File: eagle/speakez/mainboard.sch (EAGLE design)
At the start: 15 parts

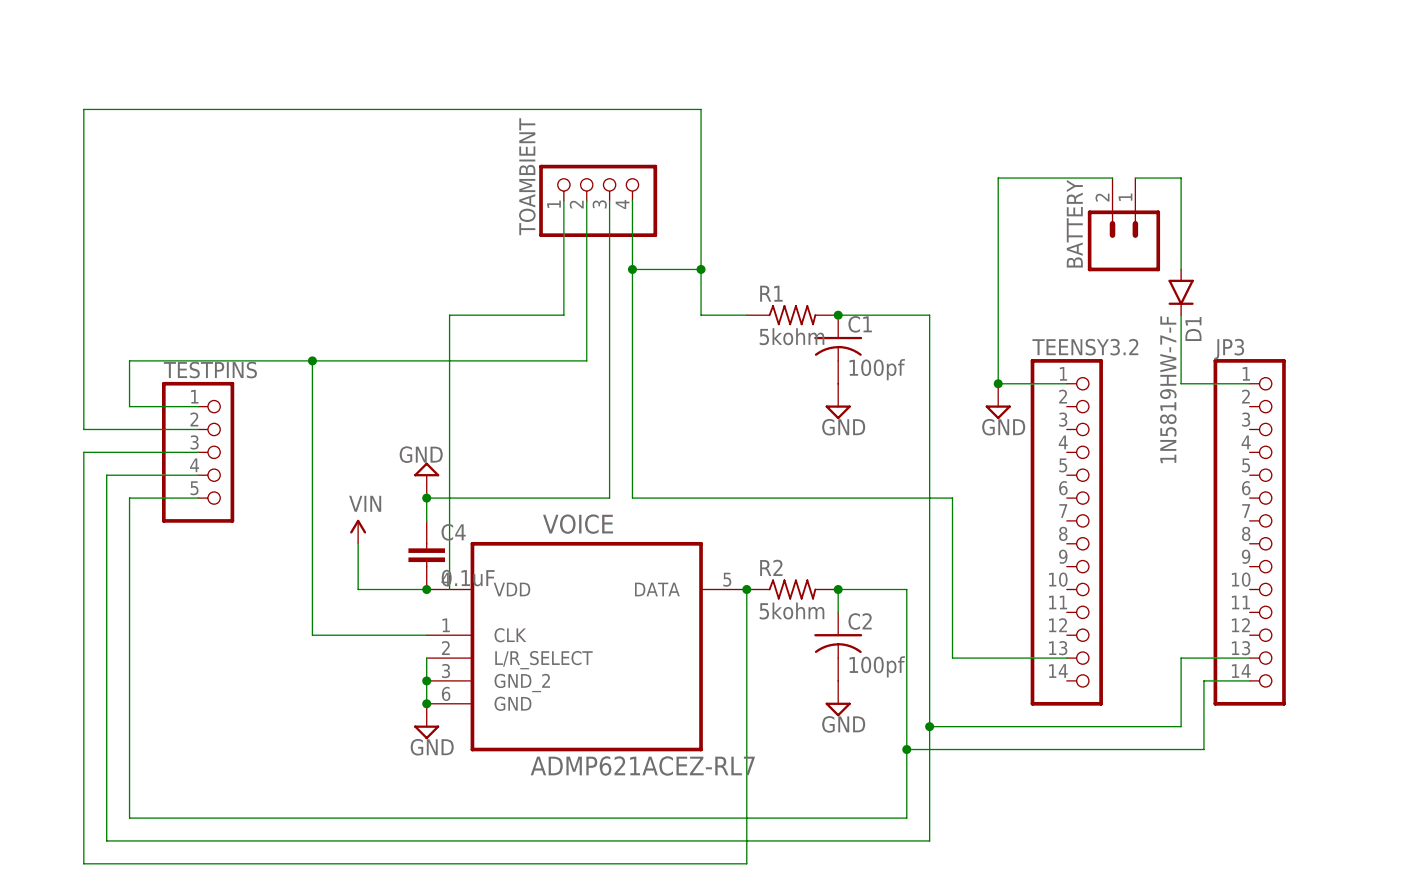
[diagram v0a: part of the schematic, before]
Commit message: remap teensy pins
move analog inputs to adc pins, switch 3.3v source, gnd source. add clk
signal to digital output pin
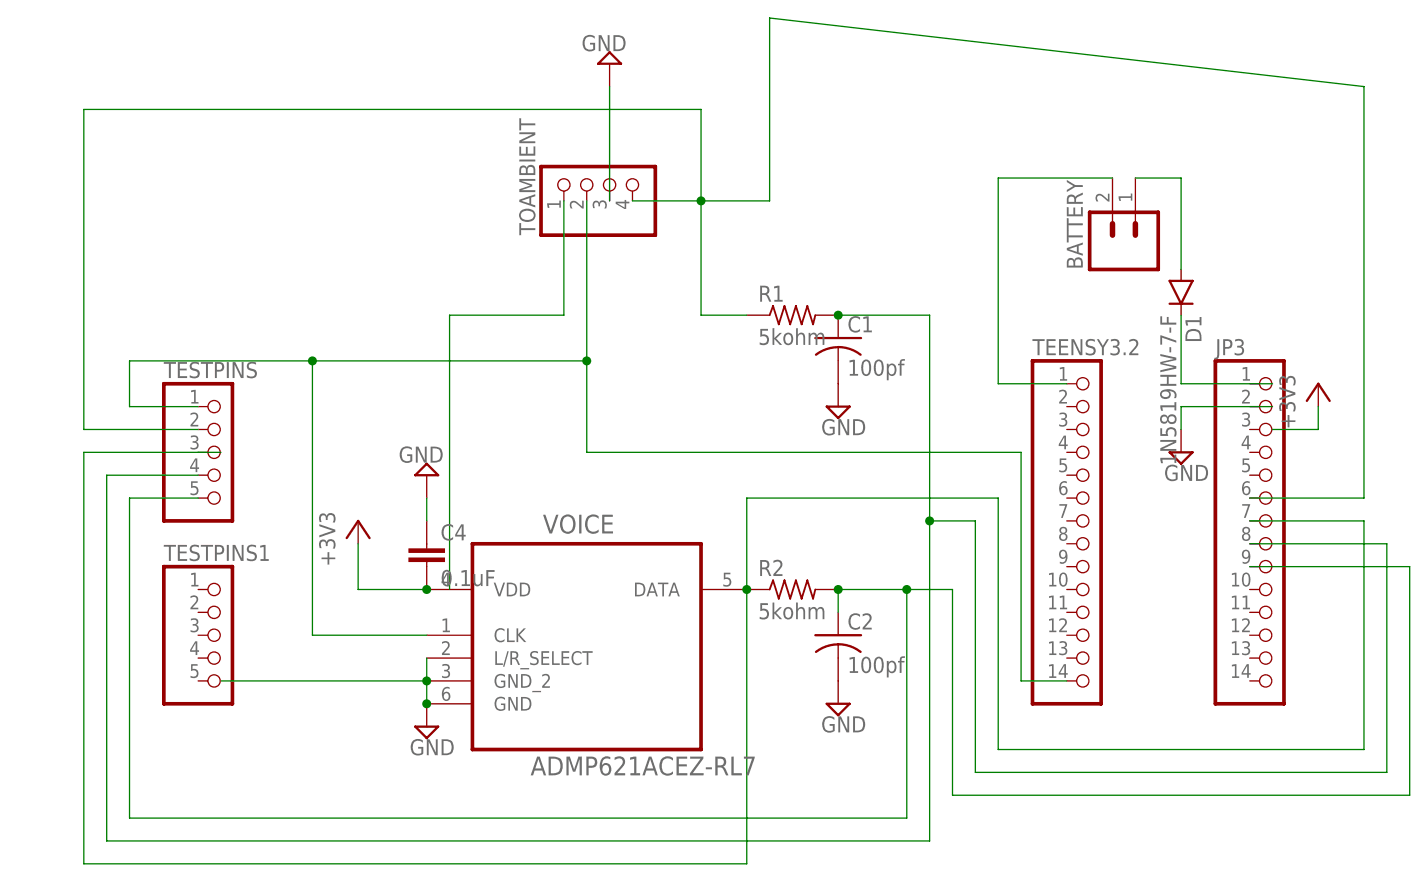
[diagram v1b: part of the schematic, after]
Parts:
- added TESTPINS1: (no value), pinhead:PINHD-1X5M
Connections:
- net VIN renamed +3V3
- new net N$13: BATTERY.2, TEENSY3.2.1
- net GND: no longer BATTERY.2, TEENSY3.2.1
- net N$1: now also JP3.8; no longer JP3.13
- net N$10: now also JP3.6; no longer TEENSY3.2.13
- net N$2: now also JP3.9; no longer JP3.14
- net N$3: no longer JP3.1
- net N$4: now also JP3.7
- net TEST-PINS: now also TEENSY3.2.14

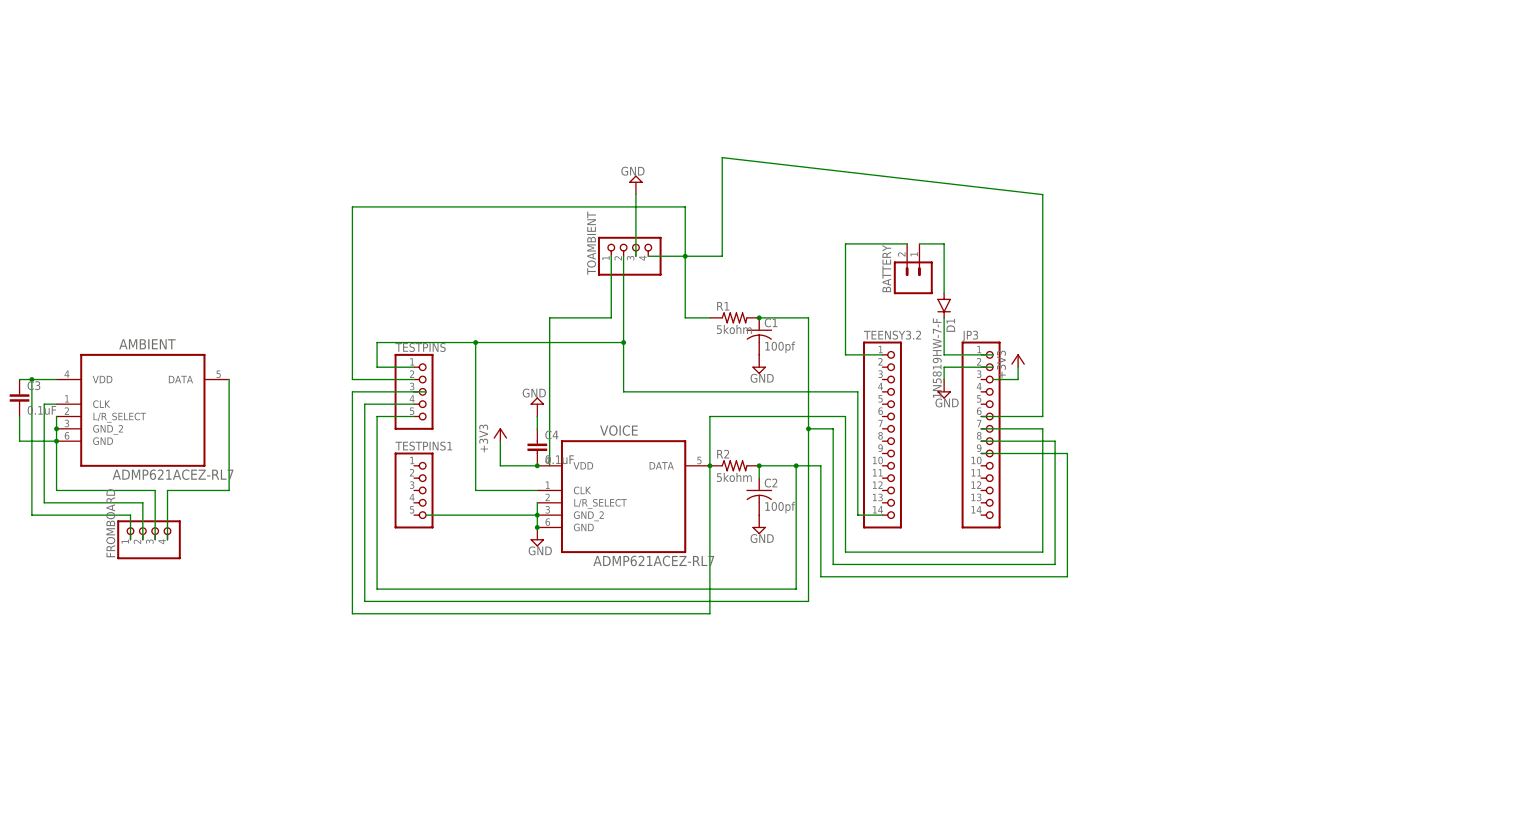
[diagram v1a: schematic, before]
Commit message: Added microcontroller
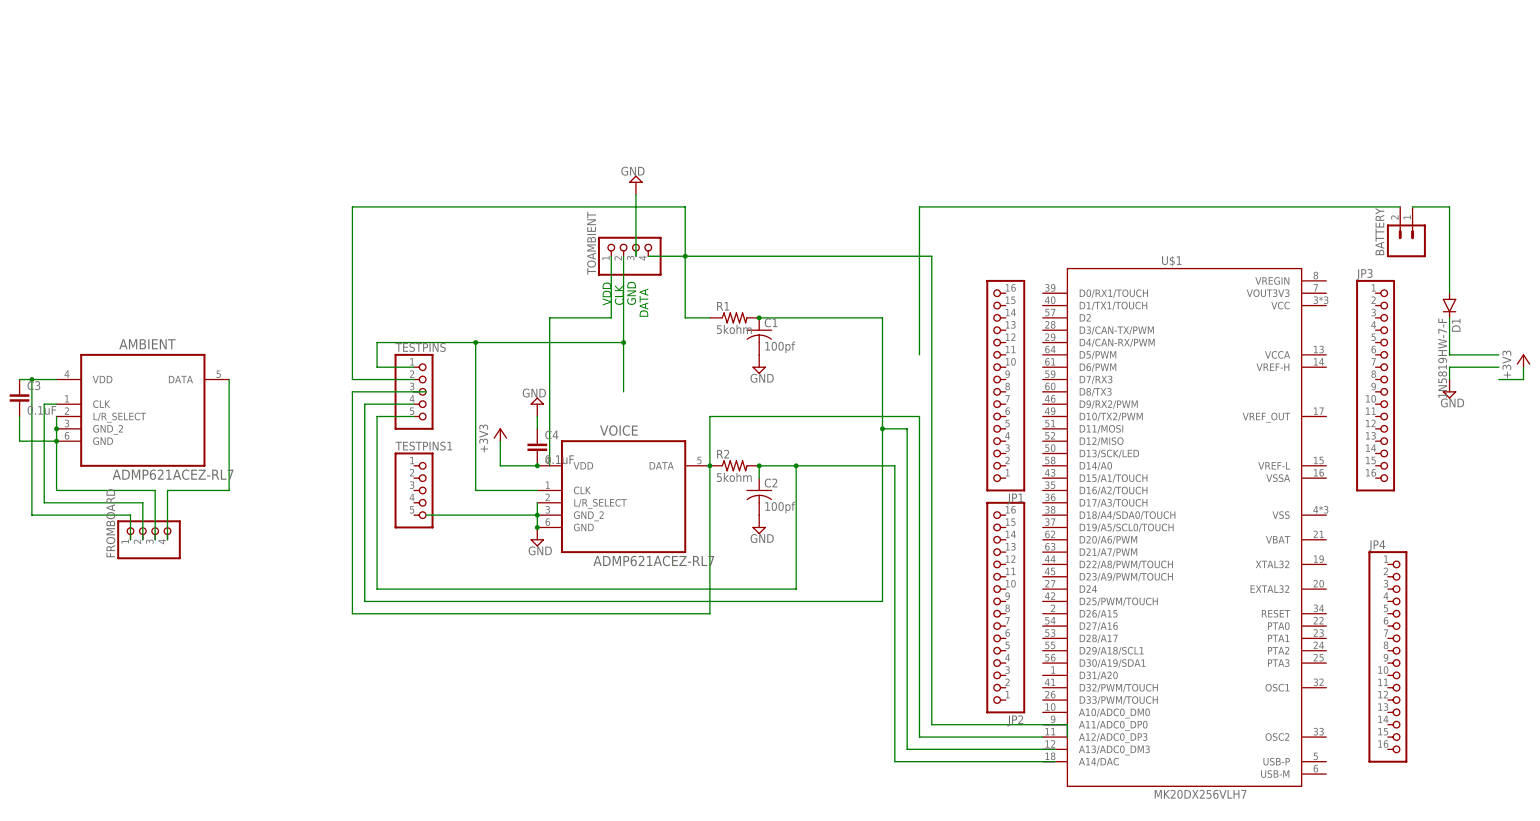
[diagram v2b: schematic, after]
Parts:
- removed TEENSY3.2: (no value), pinhead:PINHD-1X14M
- added JP1, JP2, JP4: (no value), pinhead:PINHD-1X16
- added U$1: MK20DX256VLH7, Teensy_DIY_v1.0:MK20DX256VLH7
- JP3: device pinhead:PINHD-1X14M -> pinhead:PINHD-1X16
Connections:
- net N$1: no longer JP3.8
- net N$10: no longer JP3.6
- net N$13: no longer TEENSY3.2.1
- net N$2: no longer JP3.9
- net N$4: now also U$1.A12/ADC0_DP3; no longer JP3.7
- net TEST-PINS: no longer TEENSY3.2.14
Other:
- note added: "CLK"
- note added: "DATA"
- note added: "GND"
- note added: "VDD"
- moved on the sheet: BATTERY, D1

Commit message: Added battery stuff
decoupling caps for battery with Fiona
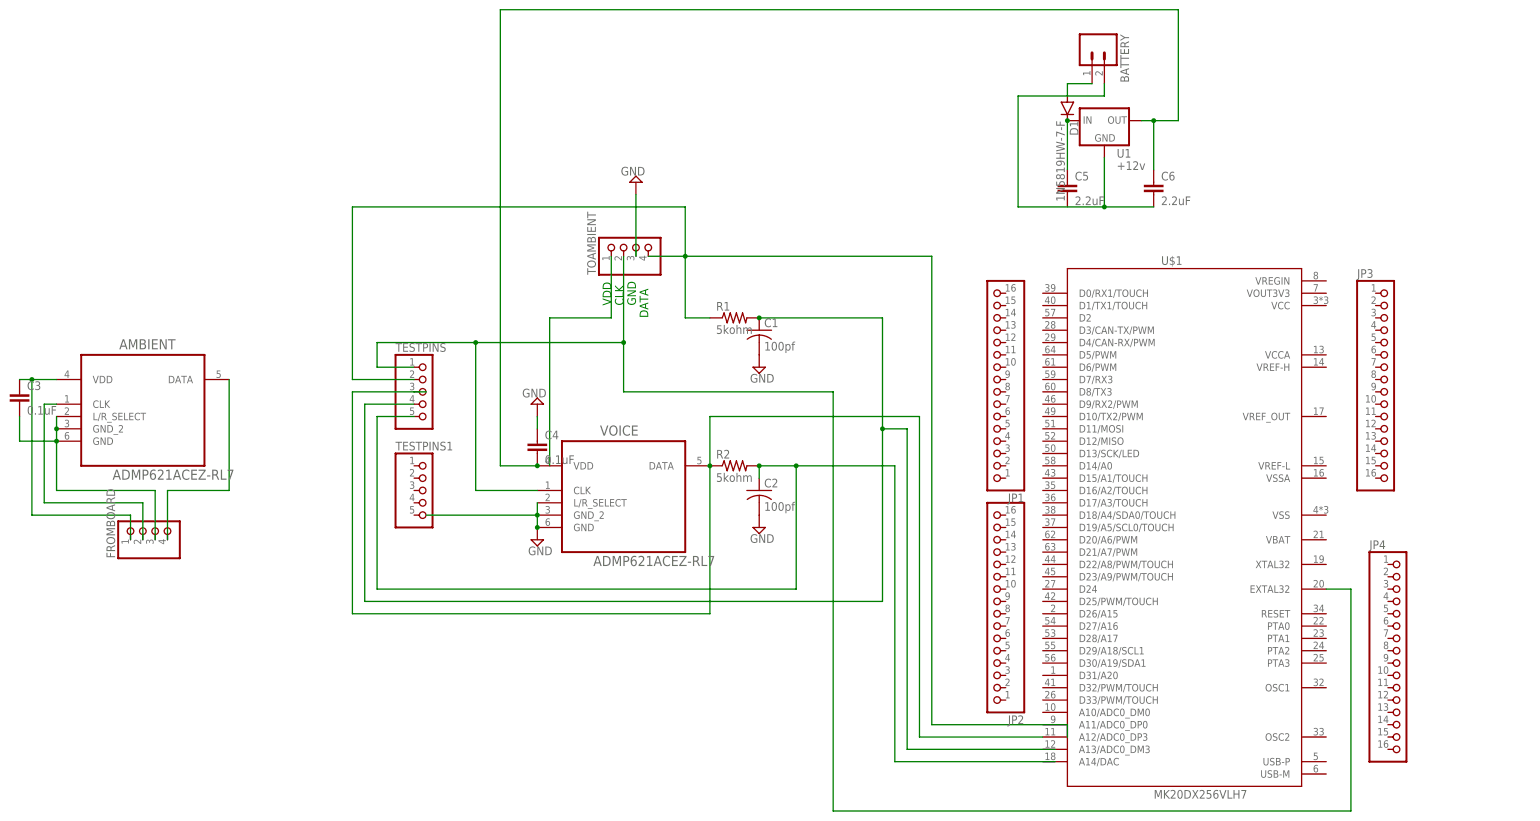
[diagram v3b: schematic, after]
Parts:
- added C5, C6: 2.2uF, SparkFun-Capacitors:CAP0805
- added U1: +12v, SparkFun-PowerIC:V_REG_78XX7812
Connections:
- net TEENSY3.2 renamed N$13
- removed net +3V3: C4.2, VOICE.VDD
- removed net N$13 (its old number): BATTERY.2
- removed net N$3: D1.C
- new net N$14: BATTERY.2, C6.2, U1.GND
- new net N$15: C5.1, D1.C, U1.IN
- new net N$16: C4.2, C6.1, U1.OUT, VOICE.VDD
- net TEST-PINS: now also U$1.EXTAL32
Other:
- moved on the sheet: BATTERY, D1
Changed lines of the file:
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@@
 <part name="D1" library="SparkFun-DiscreteSemi" deviceset="DIODE" device="SOD123" value="1N5819HW-7-F"/>
 <part name="C3" library="SparkFun-Capacitors" deviceset="CAP" device="0805" value="0.1uF"/>
-<part name="+3V1" library="supply1" deviceset="+3V3" device=""/>
-<part name="+3V2" library="supply1" deviceset="+3V3" device=""/>
-<part name="SUPPLY3" library="supply2" deviceset="GND" device=""/>
 <part name="TESTPINS1" library="pinhead" deviceset="PINHD-1X5" device="M"/>
 <part name="SUPPLY4" library="supply2" deviceset="GND" device=""/>
@@
 <part name="JP3" library="pinhead" deviceset="PINHD-1X16" device=""/>
 <part name="JP4" library="pinhead" deviceset="PINHD-1X16" device=""/>
+<part name="U1" library="SparkFun-PowerIC" deviceset="V_REG_78XX" device="7812" value="+12v"/>
+<part name="C5" library="SparkFun-Capacitors" deviceset="CAP" device="0805" value="2.2uF"/>
+<part name="C6" library="SparkFun-Capacitors" deviceset="CAP" device="0805" value="2.2uF"/>
 </parts>
 <sheets>
@@
 <instance part="FROMBOARD" gate="A" x="-66.04" y="17.78" rot="R90"/>
 <instance part="TOAMBIENT" gate="A" x="33.02" y="76.2" rot="R90"/>
-<instance part="BATTERY" gate="G$1" x="193.04" y="76.2" rot="R90"/>
-<instance part="D1" gate="G$1" x="200.66" y="63.5" rot="R270"/>
+<instance part="BATTERY" gate="G$1" x="127" y="116.84" rot="R270"/>
+<instance part="D1" gate="G$1" x="121.92" y="104.14" rot="R270"/>
 <instance part="C3" gate="G$1" x="-93.98" y="43.18"/>
-<instance part="+3V1" gate="G$1" x="5.08" y="38.1"/>
-<instance part="+3V2" gate="G$1" x="215.9" y="53.34"/>
-<instance part="SUPPLY3" gate="GND" x="200.66" y="45.72"/>
 <instance part="TESTPINS1" gate="A" x="-10.16" y="25.4"/>
 <instance part="SUPPLY4" gate="GND" x="33.02" y="88.9" rot="R180"/>
@@
 <instance part="JP3" gate="A" x="187.96" y="48.26"/>
 <instance part="JP4" gate="A" x="190.5" y="-7.62"/>
+<instance part="U1" gate="G$1" x="129.54" y="101.6"/>
+<instance part="C5" gate="G$1" x="121.92" y="86.36"/>
+<instance part="C6" gate="G$1" x="139.7" y="86.36"/>
 </instances>
 <busses>
@@
 </segment>
 <segment>
-<pinref part="SUPPLY3" gate="GND" pin="GND"/>
-<wire x1="210.82" y1="50.8" x2="200.66" y2="50.8" width="0.1524" layer="91"/>
-<wire x1="200.66" y1="50.8" x2="200.66" y2="48.26" width="0.1524" layer="91"/>
-</segment>
-<segment>
 <pinref part="TOAMBIENT" gate="A" pin="3"/>
 <pinref part="SUPPLY4" gate="GND" pin="GND"/>
@@
 <wire x1="30.48" y1="55.88" x2="30.48" y2="45.72" width="0.1524" layer="91"/>
 <junction x="30.48" y="55.88"/>
-</segment>
-</net>
-<net name="TEENSY3.2" class="0">
-<segment>
-<pinref part="BATTERY" gate="G$1" pin="1"/>
-<wire x1="193.04" y1="83.82" x2="200.66" y2="83.82" width="0.1524" layer="91"/>
-<pinref part="D1" gate="G$1" pin="A"/>
-<wire x1="200.66" y1="83.82" x2="200.66" y2="66.04" width="0.1524" layer="91"/>
+<pinref part="U$1" gate="G$1" pin="EXTAL32"/>
+<wire x1="175.26" y1="5.08" x2="180.34" y2="5.08" width="0.1524" layer="91"/>
+<wire x1="180.34" y1="5.08" x2="180.34" y2="-40.64" width="0.1524" layer="91"/>
+<wire x1="180.34" y1="-40.64" x2="73.66" y2="-40.64" width="0.1524" layer="91"/>
+<wire x1="73.66" y1="-40.64" x2="73.66" y2="45.72" width="0.1524" layer="91"/>
+<wire x1="73.66" y1="45.72" x2="30.48" y2="45.72" width="0.1524" layer="91"/>
 </segment>
 </net>
@@
 </segment>
 </net>
-<net name="N$3" class="0">
-<segment>
+<net name="N$13" class="0">
+<segment>
+<pinref part="BATTERY" gate="G$1" pin="1"/>
+<wire x1="127" y1="109.22" x2="121.92" y2="109.22" width="0.1524" layer="91"/>
+<wire x1="121.92" y1="109.22" x2="121.92" y2="106.68" width="0.1524" layer="91"/>
+<pinref part="D1" gate="G$1" pin="A"/>
+</segment>
+</net>
+<net name="N$14" class="0">
+<segment>
+<pinref part="BATTERY" gate="G$1" pin="2"/>
+<wire x1="129.54" y1="109.22" x2="129.54" y2="106.68" width="0.1524" layer="91"/>
+<wire x1="129.54" y1="106.68" x2="111.76" y2="106.68" width="0.1524" layer="91"/>
+<wire x1="111.76" y1="106.68" x2="111.76" y2="83.82" width="0.1524" layer="91"/>
+<wire x1="111.76" y1="83.82" x2="129.54" y2="83.82" width="0.1524" layer="91"/>
+<pinref part="U1" gate="G$1" pin="GND"/>
+<wire x1="129.54" y1="83.82" x2="129.54" y2="93.98" width="0.1524" layer="91"/>
+<pinref part="C6" gate="G$1" pin="2"/>
+<wire x1="129.54" y1="83.82" x2="139.7" y2="83.82" width="0.1524" layer="91"/>
+<junction x="129.54" y="83.82"/>
+</segment>
+</net>
+<net name="N$15" class="0">
+<segment>
+<pinref part="U1" gate="G$1" pin="IN"/>
 <pinref part="D1" gate="G$1" pin="C"/>
-<wire x1="200.66" y1="60.96" x2="200.66" y2="53.34" width="0.1524" layer="91"/>
-<wire x1="210.82" y1="53.34" x2="200.66" y2="53.34" width="0.1524" layer="91"/>
-</segment>
-</net>
-<net name="+3V3" class="0">
-<segment>
+<pinref part="C5" gate="G$1" pin="1"/>
+<wire x1="121.92" y1="101.6" x2="121.92" y2="91.44" width="0.1524" layer="91"/>
+<junction x="121.92" y="101.6"/>
+</segment>
+</net>
+<net name="N$16" class="0">
+<segment>
+<pinref part="U1" gate="G$1" pin="OUT"/>
+<pinref part="C6" gate="G$1" pin="1"/>
+<wire x1="137.16" y1="101.6" x2="139.7" y2="101.6" width="0.1524" layer="91"/>
+<wire x1="139.7" y1="101.6" x2="139.7" y2="91.44" width="0.1524" layer="91"/>
+<wire x1="139.7" y1="101.6" x2="144.78" y2="101.6" width="0.1524" layer="91"/>
+<wire x1="144.78" y1="101.6" x2="144.78" y2="124.46" width="0.1524" layer="91"/>
+<junction x="139.7" y="101.6"/>
 <pinref part="VOICE" gate="A" pin="VDD"/>
 <pinref part="C4" gate="G$1" pin="2"/>
 <wire x1="12.7" y1="30.48" x2="5.08" y2="30.48" width="0.1524" layer="91"/>
-<wire x1="5.08" y1="30.48" x2="5.08" y2="35.56" width="0.1524" layer="91"/>
 <junction x="12.7" y="30.48"/>
-<pinref part="+3V1" gate="G$1" pin="+3V3"/>
-</segment>
-<segment>
-<pinref part="+3V2" gate="G$1" pin="+3V3"/>
-<wire x1="210.82" y1="48.26" x2="215.9" y2="48.26" width="0.1524" layer="91"/>
-<wire x1="215.9" y1="48.26" x2="215.9" y2="50.8" width="0.1524" layer="91"/>
-</segment>
-</net>
-<net name="N$13" class="0">
-<segment>
-<pinref part="BATTERY" gate="G$1" pin="2"/>
-<wire x1="190.5" y1="83.82" x2="91.44" y2="83.82" width="0.1524" layer="91"/>
-<wire x1="91.44" y1="83.82" x2="91.44" y2="53.34" width="0.1524" layer="91"/>
-</segment>
-</net>
+<wire x1="144.78" y1="124.46" x2="5.08" y2="124.46" width="0.1524" layer="91"/>
+<wire x1="5.08" y1="124.46" x2="5.08" y2="30.48" width="0.1524" layer="91"/>
+</segment>
+</net>

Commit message: Added clock pin
Still need to connect up headers but I can do that later
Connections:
- net N$14: now also U$1.VSS
- net N$16: now also U$1.VCC, U$1.VOUT3V3
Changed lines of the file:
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@@
 <wire x1="129.54" y1="83.82" x2="139.7" y2="83.82" width="0.1524" layer="91"/>
 <junction x="129.54" y="83.82"/>
+<wire x1="139.7" y1="83.82" x2="205.74" y2="83.82" width="0.1524" layer="91"/>
+<junction x="139.7" y="83.82"/>
+<wire x1="205.74" y1="83.82" x2="205.74" y2="20.32" width="0.1524" layer="91"/>
+<pinref part="U$1" gate="G$1" pin="VSS"/>
+<wire x1="205.74" y1="20.32" x2="175.26" y2="20.32" width="0.1524" layer="91"/>
 </segment>
 </net>
@@
 <wire x1="144.78" y1="124.46" x2="5.08" y2="124.46" width="0.1524" layer="91"/>
 <wire x1="5.08" y1="124.46" x2="5.08" y2="30.48" width="0.1524" layer="91"/>
+<wire x1="144.78" y1="101.6" x2="177.8" y2="101.6" width="0.1524" layer="91"/>
+<wire x1="177.8" y1="101.6" x2="177.8" y2="66.04" width="0.1524" layer="91"/>
+<pinref part="U$1" gate="G$1" pin="VCC"/>
+<wire x1="177.8" y1="66.04" x2="177.8" y2="63.5" width="0.1524" layer="91"/>
+<wire x1="177.8" y1="63.5" x2="175.26" y2="63.5" width="0.1524" layer="91"/>
+<pinref part="U$1" gate="G$1" pin="VOUT3V3"/>
+<wire x1="175.26" y1="66.04" x2="177.8" y2="66.04" width="0.1524" layer="91"/>
+<junction x="177.8" y="66.04"/>
 </segment>
 </net>
